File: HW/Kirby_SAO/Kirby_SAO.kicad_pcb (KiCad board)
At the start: 2 copper layers, 45.9 x 43.9 mm, 19 parts, among them X1 Badgelife_sao_connector_v169b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

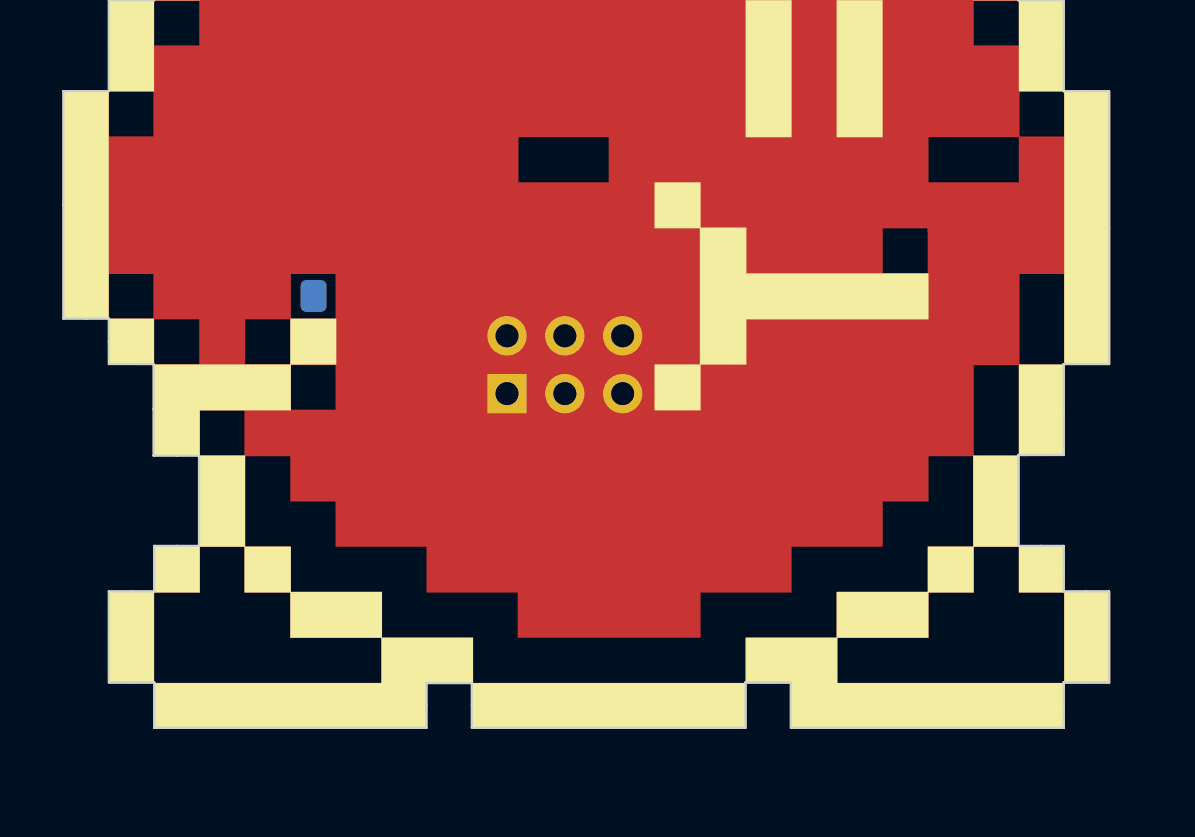
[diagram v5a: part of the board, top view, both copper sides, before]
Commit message: B.Cu ground pour.
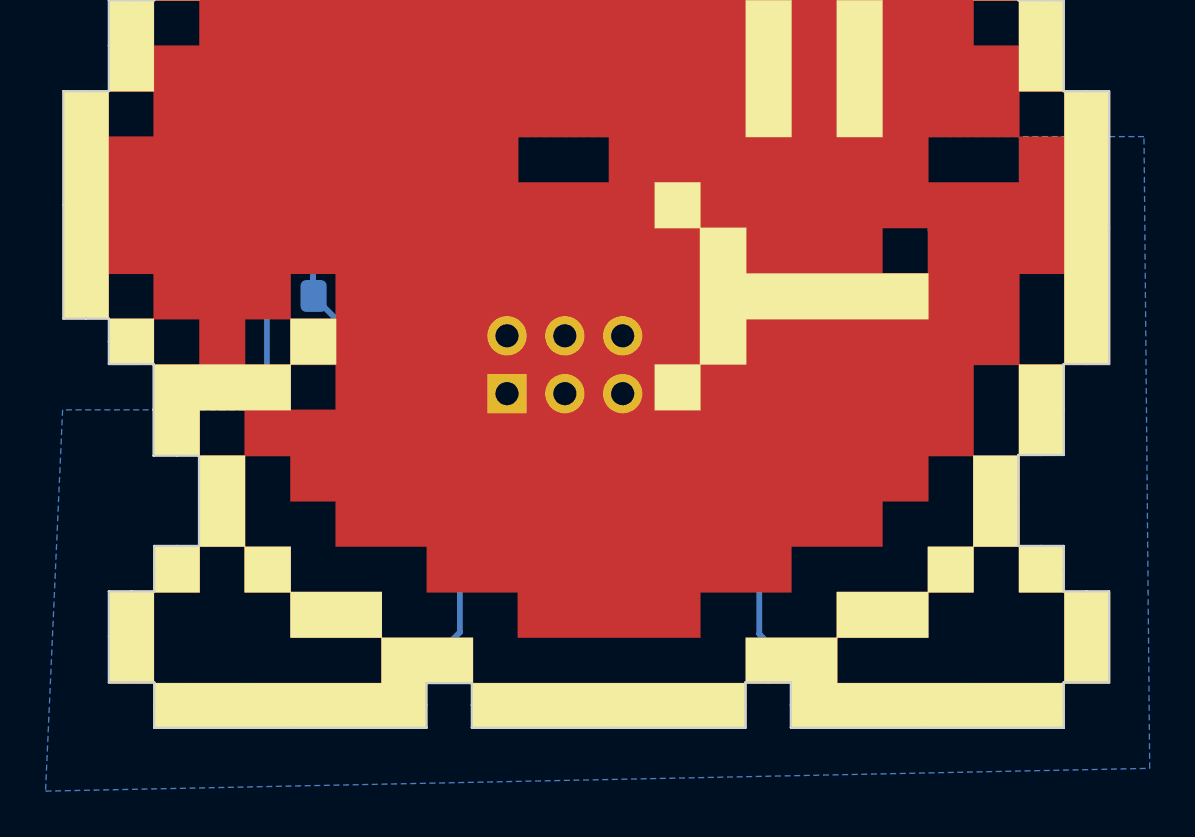
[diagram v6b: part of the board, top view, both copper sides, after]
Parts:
- turned R1 to 180 degrees
- turned R2 to 180 degrees
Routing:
- net Net-(D1-Pad2): track 0.00 -> 62.4 mm
- net Net-(D10-Pad2): track 0.00 -> 48.8 mm
- net VCC: track 5.00 -> 33.3 mm
- added copper zone on B.Cu, net GND
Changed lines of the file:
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@@
   (general
     (thickness 1.6)
-    (drawings 119)
-    (tracks 2)
+    (drawings 118)
+    (tracks 45)
     (zones 0)
     (modules 19)
@@
     (37 F.SilkS user hide)
     (38 B.Mask user)
-    (39 F.Mask user)
+    (39 F.Mask user hide)
     (40 Dwgs.User user hide)
     (41 Cmts.User user hide)
@@
   )
   (setup
-    (last_trace_width 0.254)
+    (last_trace_width 0.1778)
     (user_trace_width 0.1778)
     (user_trace_width 0.2032)
     (user_trace_width 0.254)
     (trace_clearance 0.1778)
-    (zone_clearance 0.508)
+    (zone_clearance 0.01)
     (zone_45_only no)
     (trace_min 0.1778)
@@
   )
   (module Resistor_SMD:R_0805_2012Metric_Pad1.15x1.40mm_HandSolder (layer B.Cu)
-    (at 87 98)
+    (at 87 98 180)
     (descr "Resistor SMD 0805 (2012 Metric), square (rectangular) end terminal, IPC_7351 nominal with elongated pad for handsoldering. (Body size source: https://docs.google.com/spreadsheets/d/1BsfQQcO9C6DZCsRaXUlFlo91Tg2WpOkGARC1WS5S8t0/edit?usp=sharing), generated with kicad-footprint-generator")
     (tags "resistor handsolder")
     (attr smd)
-    (fp_text reference R1 (at 0 1.65) (layer B.SilkS)
+    (fp_text reference R1 (at 0 -1.75) (layer B.SilkS)
       (effects (font (size 1 1) (thickness 0.15)) (justify mirror))
     )
@@
     (fp_line (start -1 0.6) (end 1 0.6) (layer B.Fab) (width 0.1))
     (fp_line (start -1 -0.6) (end -1 0.6) (layer B.Fab) (width 0.1))
-    (pad 2 smd roundrect (at 1.025 0) (size 1.15 1.4) (layers B.Cu B.Paste B.Mask) (roundrect_rratio 0.217391)
+    (pad 2 smd roundrect (at 1.025 0 180) (size 1.15 1.4) (layers B.Cu B.Paste B.Mask) (roundrect_rratio 0.217391)
       (net 2 "Net-(D1-Pad2)"))
-    (pad 1 smd roundrect (at -1.025 0) (size 1.15 1.4) (layers B.Cu B.Paste B.Mask) (roundrect_rratio 0.217391)
+    (pad 1 smd roundrect (at -1.025 0 180) (size 1.15 1.4) (layers B.Cu B.Paste B.Mask) (roundrect_rratio 0.217391)
       (net 3 VCC))
     (model ${KISYS3DMOD}/Resistor_SMD.3dshapes/R_0805_2012Metric.wrl
@@
   )
   (module Resistor_SMD:R_0805_2012Metric_Pad1.15x1.40mm_HandSolder (layer B.Cu)
-    (at 87 103)
+    (at 87 103 180)
     (descr "Resistor SMD 0805 (2012 Metric), square (rectangular) end terminal, IPC_7351 nominal with elongated pad for handsoldering. (Body size source: https://docs.google.com/spreadsheets/d/1BsfQQcO9C6DZCsRaXUlFlo91Tg2WpOkGARC1WS5S8t0/edit?usp=sharing), generated with kicad-footprint-generator")
     (tags "resistor handsolder")
     (attr smd)
-    (fp_text reference R2 (at 0 1.65) (layer B.SilkS)
+    (fp_text reference R2 (at 0 -1.75) (layer B.SilkS)
       (effects (font (size 1 1) (thickness 0.15)) (justify mirror))
     )
@@
     (fp_line (start -1 0.6) (end 1 0.6) (layer B.Fab) (width 0.1))
     (fp_line (start -1 -0.6) (end -1 0.6) (layer B.Fab) (width 0.1))
-    (pad 2 smd roundrect (at 1.025 0) (size 1.15 1.4) (layers B.Cu B.Paste B.Mask) (roundrect_rratio 0.217391)
+    (pad 2 smd roundrect (at 1.025 0 180) (size 1.15 1.4) (layers B.Cu B.Paste B.Mask) (roundrect_rratio 0.217391)
       (net 2 "Net-(D1-Pad2)"))
-    (pad 1 smd roundrect (at -1.025 0) (size 1.15 1.4) (layers B.Cu B.Paste B.Mask) (roundrect_rratio 0.217391)
+    (pad 1 smd roundrect (at -1.025 0 180) (size 1.15 1.4) (layers B.Cu B.Paste B.Mask) (roundrect_rratio 0.217391)
       (net 3 VCC))
     (model ${KISYS3DMOD}/Resistor_SMD.3dshapes/R_0805_2012Metric.wrl
@@
     )
   )
-  (gr_circle (center 143.2 115.6) (end 148.2 115.6) (layer B.SilkS) (width 0.12))
   (gr_line (start 81.027496 120.968159) (end 81.027496 119.969607) (layer Edge.Cuts) (width 0.1))
   (gr_line (start 81.027496 119.969607) (end 80.028944 119.969607) (layer Edge.Cuts) (width 0.1))
@@
   (gr_line (start 81.027496 120.968159) (end 81.027496 120.968159) (layer Edge.Cuts) (width 0.1))
   (gr_line (start 81.027496 120.968159) (end 81.027496 120.968159) (layer Edge.Cuts) (width 0.1))
-  (segment (start 85.975 102.2) (end 85.975 98) (width 0.254) (layer B.Cu) (net 3))
-  (segment (start 85.975 103) (end 85.975 102.2) (width 0.254) (layer B.Cu) (net 3))
+  (segment (start 85.975 98) (end 85.975 103) (width 0.254) (layer B.Cu) (net 2))
+  (segment (start 85.975 107.725) (end 85.975 103.8) (width 0.254) (layer B.Cu) (net 2))
+  (segment (start 85.975 103.8) (end 85.975 103) (width 0.254) (layer B.Cu) (net 2))
+  (segment (start 88.75 110.5) (end 85.975 107.725) (width 0.254) (layer B.Cu) (net 2))
+  (segment (start 89.8 110.5) (end 88.75 110.5) (width 0.254) (layer B.Cu) (net 2))
+  (segment (start 97.5 99.8) (end 96.9 99.8) (width 0.254) (layer B.Cu) (net 2))
+  (segment (start 86.598372 97.376628) (end 85.975 98) (width 0.254) (layer B.Cu) (net 2))
+  (segment (start 87.225 96.75) (end 86.598372 97.376628) (width 0.254) (layer B.Cu) (net 2))
+  (segment (start 96.9 99.8) (end 93.85 96.75) (width 0.254) (layer B.Cu) (net 2))
+  (segment (start 93.85 96.75) (end 87.225 96.75) (width 0.254) (layer B.Cu) (net 2))
+  (segment (start 92.95 112.45) (end 92.75 112.25) (width 0.254) (layer B.Cu) (net 2))
+  (segment (start 99.954595 117.025305) (end 100.343503 116.636397) (width 0.254) (layer B.Cu) (net 2))
+  (segment (start 100.343503 116.636397) (end 100.343503 115.093503) (width 0.254) (layer B.Cu) (net 2))
+  (segment (start 100.343503 115.093503) (end 97.7 112.45) (width 0.254) (layer B.Cu) (net 2))
+  (segment (start 92.75 111.75) (end 92.75 112.25) (width 0.254) (layer B.Cu) (net 2))
+  (segment (start 91.5 110.5) (end 92.75 111.75) (width 0.254) (layer B.Cu) (net 2))
+  (segment (start 89.8 110.5) (end 91.5 110.5) (width 0.254) (layer B.Cu) (net 2))
+  (segment (start 97.7 112.45) (end 94.45 112.45) (width 0.254) (layer B.Cu) (net 2))
+  (segment (start 94.45 112.45) (end 92.95 112.45) (width 0.254) (layer B.Cu) (net 2))
+  (segment (start 82 120.45) (end 82.8 121.25) (width 0.254) (layer B.Cu) (net 2))
+  (segment (start 82.8 121.25) (end 90.972595 121.25) (width 0.254) (layer B.Cu) (net 2))
+  (segment (start 90.972595 121.25) (end 94.45 117.772595) (width 0.254) (layer B.Cu) (net 2))
+  (segment (start 94.45 117.772595) (end 94.45 112.45) (width 0.254) (layer B.Cu) (net 2))
+  (segment (start 88 102.2) (end 88 98) (width 0.254) (layer B.Cu) (net 3))
+  (segment (start 88 103) (end 88 102.2) (width 0.254) (layer B.Cu) (net 3))
+  (segment (start 109.975 102.775) (end 109.975 98) (width 0.254) (layer B.Cu) (net 3))
+  (segment (start 98.27 103) (end 109.75 103) (width 0.254) (layer B.Cu) (net 3))
+  (segment (start 109.75 103) (end 109.975 102.775) (width 0.254) (layer B.Cu) (net 3))
+  (segment (start 96.52 104.75) (end 98.27 103) (width 0.254) (layer B.Cu) (net 3))
+  (segment (start 89.75 104.75) (end 88 103) (width 0.254) (layer B.Cu) (net 3))
+  (segment (start 96.52 104.75) (end 89.75 104.75) (width 0.254) (layer B.Cu) (net 3))
+  (segment (start 112.025 98) (end 112.025 103) (width 0.254) (layer B.Cu) (net 8))
+  (segment (start 113.825 99.8) (end 112.025 98) (width 0.254) (layer B.Cu) (net 8))
+  (segment (start 115.5 99.8) (end 113.825 99.8) (width 0.254) (layer B.Cu) (net 8))
+  (segment (start 112.121321 103) (end 112.025 103) (width 0.254) (layer B.Cu) (net 8))
+  (segment (start 116.275305 107.153984) (end 112.121321 103) (width 0.254) (layer B.Cu) (net 8))
+  (segment (start 110.410966 108.789645) (end 110.389645 108.789645) (width 0.254) (layer B.Cu) (net 8))
+  (segment (start 112.525305 110.903984) (end 110.410966 108.789645) (width 0.254) (layer B.Cu) (net 8))
+  (segment (start 110.389645 108.789645) (end 114.079289 105.1) (width 0.254) (layer B.Cu) (net 8))
+  (segment (start 104.275305 114.903984) (end 107.589645 111.589645) (width 0.254) (layer B.Cu) (net 8))
+  (segment (start 107.589645 111.589645) (end 110.389645 108.789645) (width 0.254) (layer B.Cu) (net 8))
+  (segment (start 107.6 111.6) (end 107.589645 111.589645) (width 0.254) (layer B.Cu) (net 8))
+  (segment (start 107.6 117.85) (end 107.6 111.6) (width 0.254) (layer B.Cu) (net 8))
+  (segment (start 110.2 120.45) (end 107.6 117.85) (width 0.254) (layer B.Cu) (net 8))
+  (segment (start 117 120.45) (end 110.2 120.45) (width 0.254) (layer B.Cu) (net 8))
   (zone (net 0) (net_name "") (layer B.Cu) (hatch full 0.508)
     (connect_pads (clearance 0.508))
     (min_thickness 0.254)
-    (keepout (tracks not_allowed) (vias not_allowed) (copperpour allowed))
+    (keepout (tracks not_allowed) (vias not_allowed) (copperpour not_allowed))
     (fill (arc_segments 32) (thermal_gap 0.508) (thermal_bridge_width 0.508))
     (polygon
@@
     (connect_pads (clearance 0.508))
     (min_thickness 0.254)
-    (keepout (tracks not_allowed) (vias not_allowed) (copperpour allowed))
+    (keepout (tracks not_allowed) (vias not_allowed) (copperpour not_allowed))
     (fill (arc_segments 32) (thermal_gap 0.508) (thermal_bridge_width 0.508))
     (polygon
@@
       )
     )
+  )
+  (zone (net 1) (net_name GND) (layer B.Cu) (hatch edge 0.508)
+    (connect_pads (clearance 0.01))
+    (min_thickness 0.0254)
+    (fill yes (arc_segments 32) (thermal_gap 0.508) (thermal_bridge_width 0.508))
+    (polygon
+      (pts
+        (xy 124.5 96) (xy 84.75 96) (xy 85 108) (xy 77 108) (xy 76.25 124.75)
+        (xy 124.75 123.75)
+      )
+    )
